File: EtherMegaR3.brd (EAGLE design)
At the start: 101.6 x 53.3 mm, 120 parts, among them IC1 EUP3476SO08T, IC2 APX811-44UG-7, IC3 ATMEGA16U2-MU, IC4 MCP24AA025E48, IC6 W5100SQFP80, IC9 ATMEGA2560-16AU, J1 DC_2_1MM, P1 USB-6PSMT, P3 ICSP:USB, P4 microSD, Q2 2N7002, Q3 2N7002, U1 HY931147C-RJ45, X1 16MHz, X2 25MHz, X3 16MHz

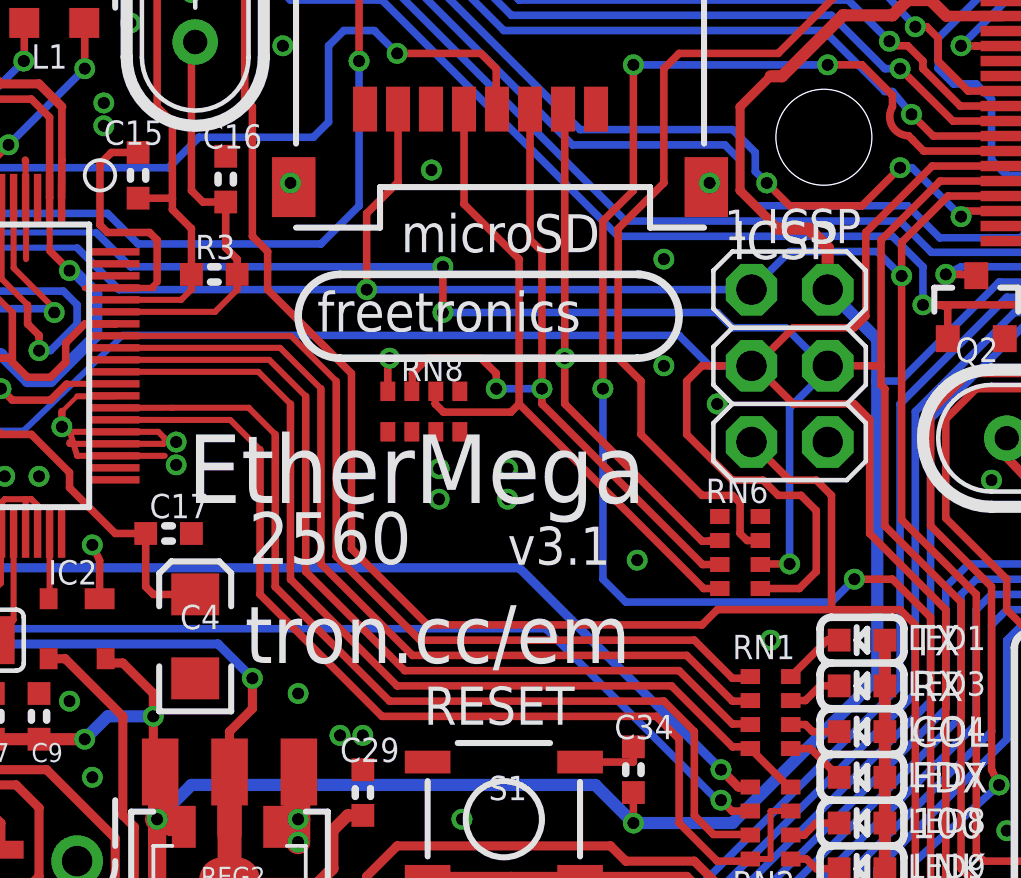
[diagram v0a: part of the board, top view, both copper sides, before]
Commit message: Changed branding to SuperHouse for v3.1 release
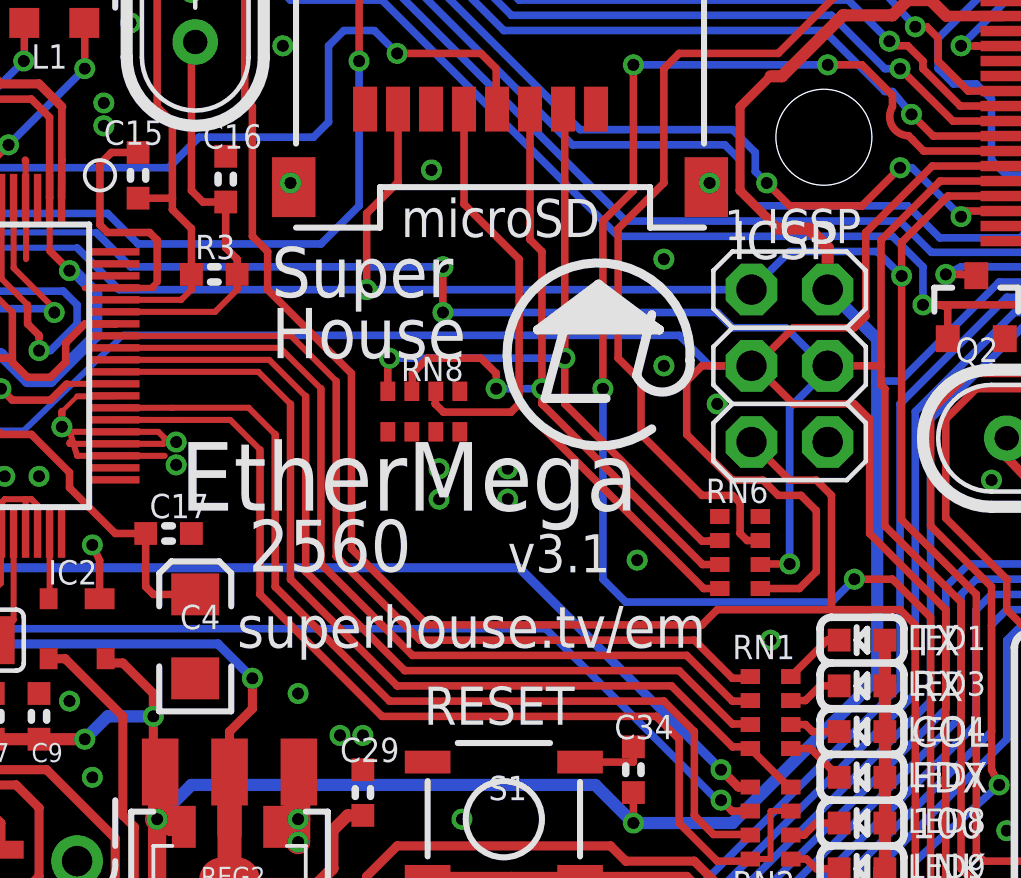
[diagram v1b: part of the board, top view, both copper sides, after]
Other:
- board text added: "House"
- board text added: "Super"
- board text added: "SuperHouse"
- board text added: "by Jonathan Oxer and Marc Alexander"
- board text added: "superhouse.tv/em"
- board text added: "www.superhouse.tv/em"
- board text removed: "by Marc Alexander and Jonathan Oxer"
- board text removed: "freetronics"
- board text removed: "tron.cc/em"
- board text removed: "v3.0"
- board text removed: "www.freetronics.com/em"

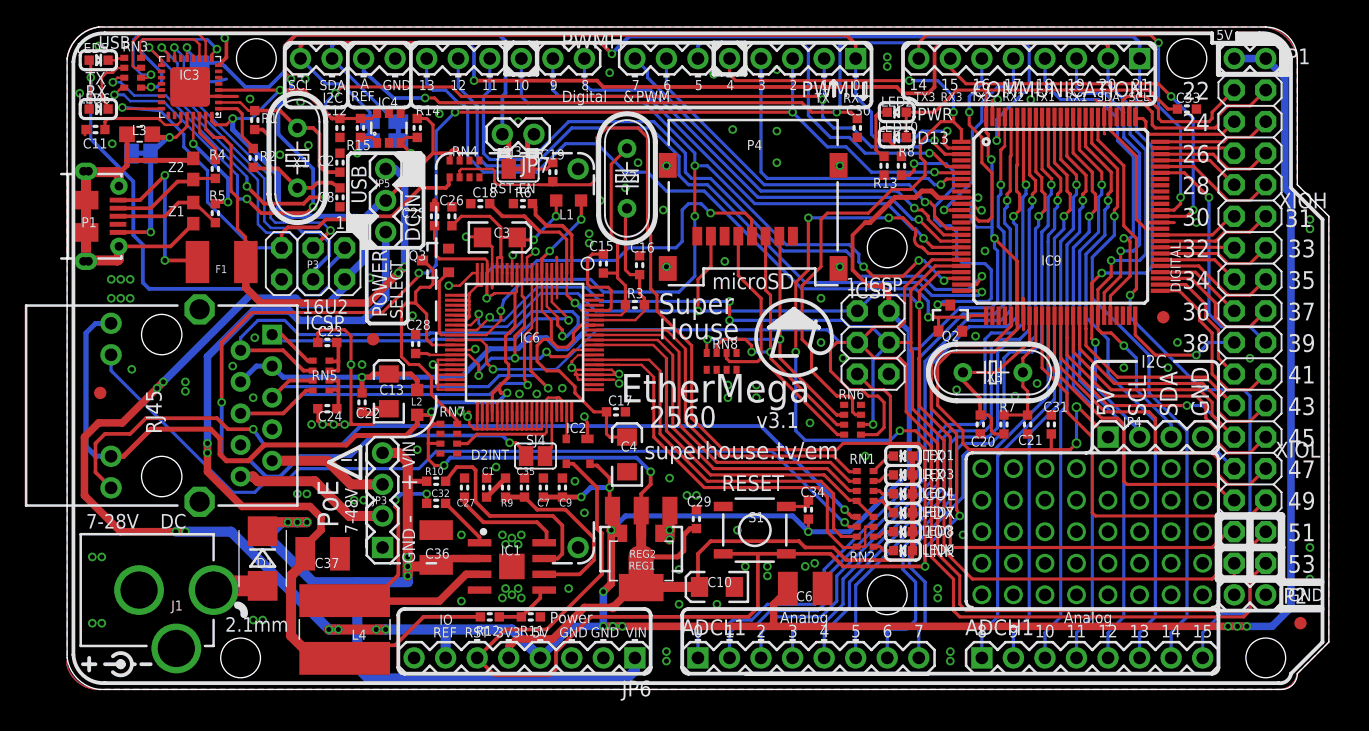
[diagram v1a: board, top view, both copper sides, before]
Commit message: Part replacement using SuperHouse libraries
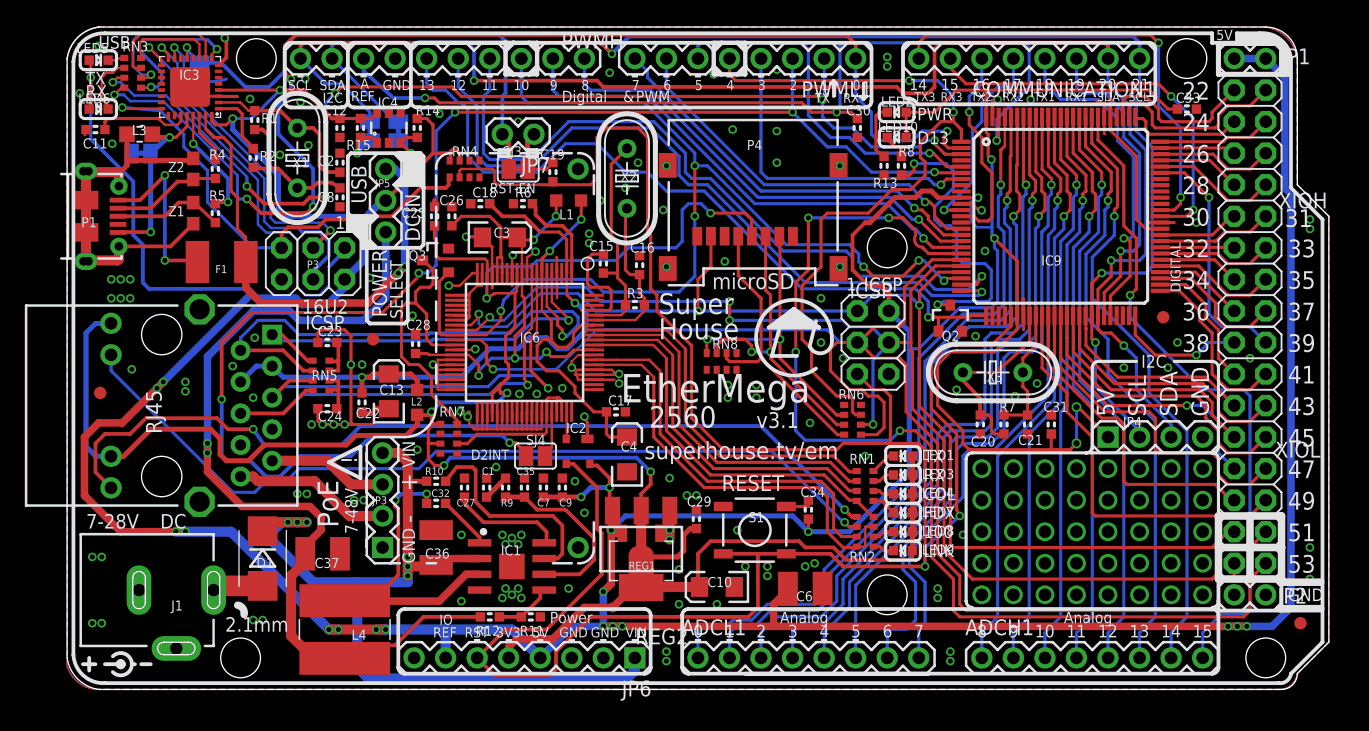
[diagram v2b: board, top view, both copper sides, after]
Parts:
- ADCH1, ADCL1, COMMUNICATION1, PWML1: value (none) -> M08-SOCKET; device freetronics-master-v1.1:1X08 -> SuperHouse-Connectors:1X08-S
- C1, C12, C15, C16, C17, C19, C2, C20, C21, C22, C23, C24, C25, C26, C27, C28, C29, C30, C31, C32, C33, C34, C35, C7, C8, C9: device freetronics-marc:0603 -> SuperHouse-DiscreteSemi:C0603
- C11: device freetronics-master-v1:0603 -> SuperHouse-DiscreteSemi:C0603
- C13, C3, C4: device freetronics:EIA3216 -> SuperHouse-DiscreteSemi:EIA3216
- F1: device rcl:L1812 -> SuperHouse-Fuses:1812
- IC3: device freetronics-jon:ATMEL_QFN32 -> SuperHouse-MCUs:ATMEL_QFN32
- IC6: device freetronics-marc:SQFP80 -> SuperHouse-ICs:SQFP80
- J1: device freetronics:POWER_JACK_PTH -> SuperHouse-Connectors:POWER_JACK_SLOTS
- JP5: device freetronics-master-v1.1:1X03 -> SuperHouse-Connectors:1X03-P
- LED1, LED10, LED2, LED3, LED4, LED5, LED6, LED7, LED8, LED9: device freetronics-jon:LED-0603 -> SuperHouse-LEDs:LED-0603
- P1: value USB-6PSMT -> USB-6P-SMT; device freetronics-jon:USB-MICROB-MB05PMXX -> SuperHouse-Connectors:USB-MICROB-MB05PMXX
- Q2, Q3: device freetronics:SOT23-3 -> SuperHouse-DiscreteSemi:SOT23-3
- R1, R13, R2, R3, R4, R5, R6, R7, R8: device freetronics-marc:0603 -> SuperHouse-DiscreteSemi:R0603
- R10, R11, R9: device freetronics-original:0603 -> SuperHouse-DiscreteSemi:R0603
- R14, R15: device freetronics-master-v1.1:0603 -> SuperHouse-DiscreteSemi:R0603
- REG2: device freetronics:SOT223 -> SuperHouse-Regulators:SOT-223
- RN1, RN2, RN3, RN5, RN6, RN7, RN8: device freetronics-master-v1:CAY16 -> SuperHouse-DiscreteSemi:CAY16
- S1: device freetronics:TACTILE_SWITCH_SMD -> SuperHouse-Switches:TACTILE_SMD-6MM
- U1: device freetronics-jon:HY931147C -> SuperHouse-Connectors:HY931147C
- X1, X2, X3: device freetronics-master-v1:HC49U-V -> SuperHouse-Oscillators:HC49U-V
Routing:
- net 3V3D: track 194.2 -> 196.3 mm
- net GND: track 138.7 -> 140.2 mm
